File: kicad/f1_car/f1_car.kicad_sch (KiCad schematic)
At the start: 3 parts, among them U1 ESP32-DevKitC

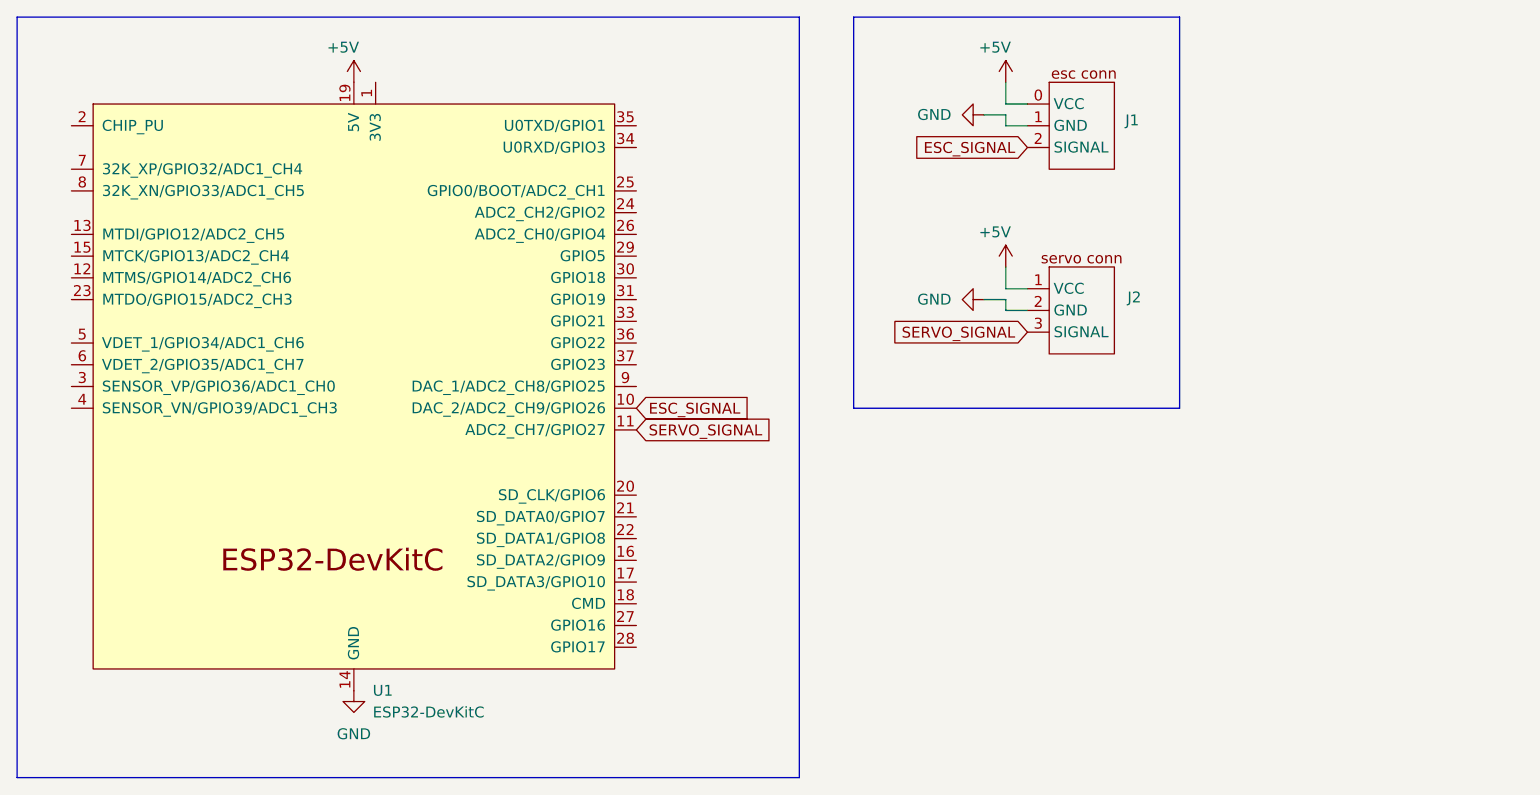
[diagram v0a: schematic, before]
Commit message: added limiter
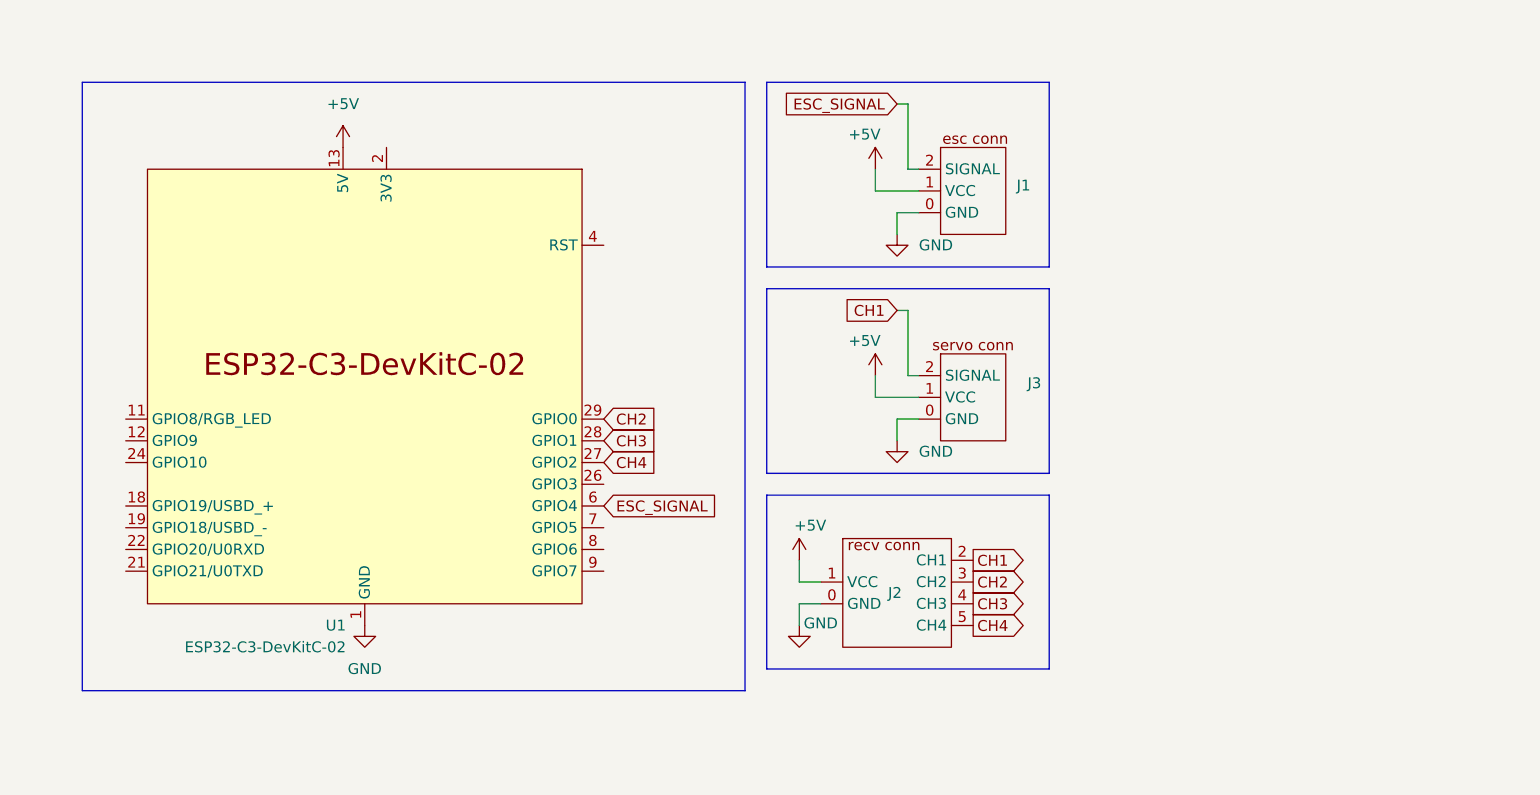
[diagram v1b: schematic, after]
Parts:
- removed J2: ~, symbol lib_progetto:steering_servo_connector
- removed U1: ESP32-DevKitC, PCM_Espressif:ESP32-DevKitC, symbol PCM_Espressif:ESP32-DevKitC
- added J2: ~, symbol lib_progetto:receiver_connector
- added J3: ~, symbol lib_progetto:steering_servo_connector
- added U1: ESP32-C3-DevKitC-02, PCM_Espressif:ESP32-C3-DevKitC-02, symbol PCM_Espressif:ESP32-C3-DevKitC-02
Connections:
- net +5V: now also J1.1 (VCC), J2.1 (VCC), J3.1 (VCC), U1.13 (5V), U1.14 (5V); no longer J1.0 (VCC)
- net ESC_SIGNAL: now also U1.6 (GPIO4)
- net GND: now also J1.0 (GND), J2.0 (GND), J3.0 (GND), U1.1 (GND), U1.10 (GND), U1.15 (GND), U1.16 (GND), U1.17 (GND), U1.20 (GND), U1.23 (GND), U1.25 (GND), U1.30 (GND), U1.5 (GND); no longer J1.1 (GND)
- new net 3V3: U1.2 (3V3), U1.3 (3V3)
- new net CH1: J2.2 (CH1), J3.2 (SIGNAL)
- new net CH2: J2.3 (CH2), U1.29 (GPIO0)
- new net CH3: J2.4 (CH3), U1.28 (GPIO1)
- new net CH4: J2.5 (CH4), U1.27 (GPIO2)
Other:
- moved on the sheet: J1

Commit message: schematic update
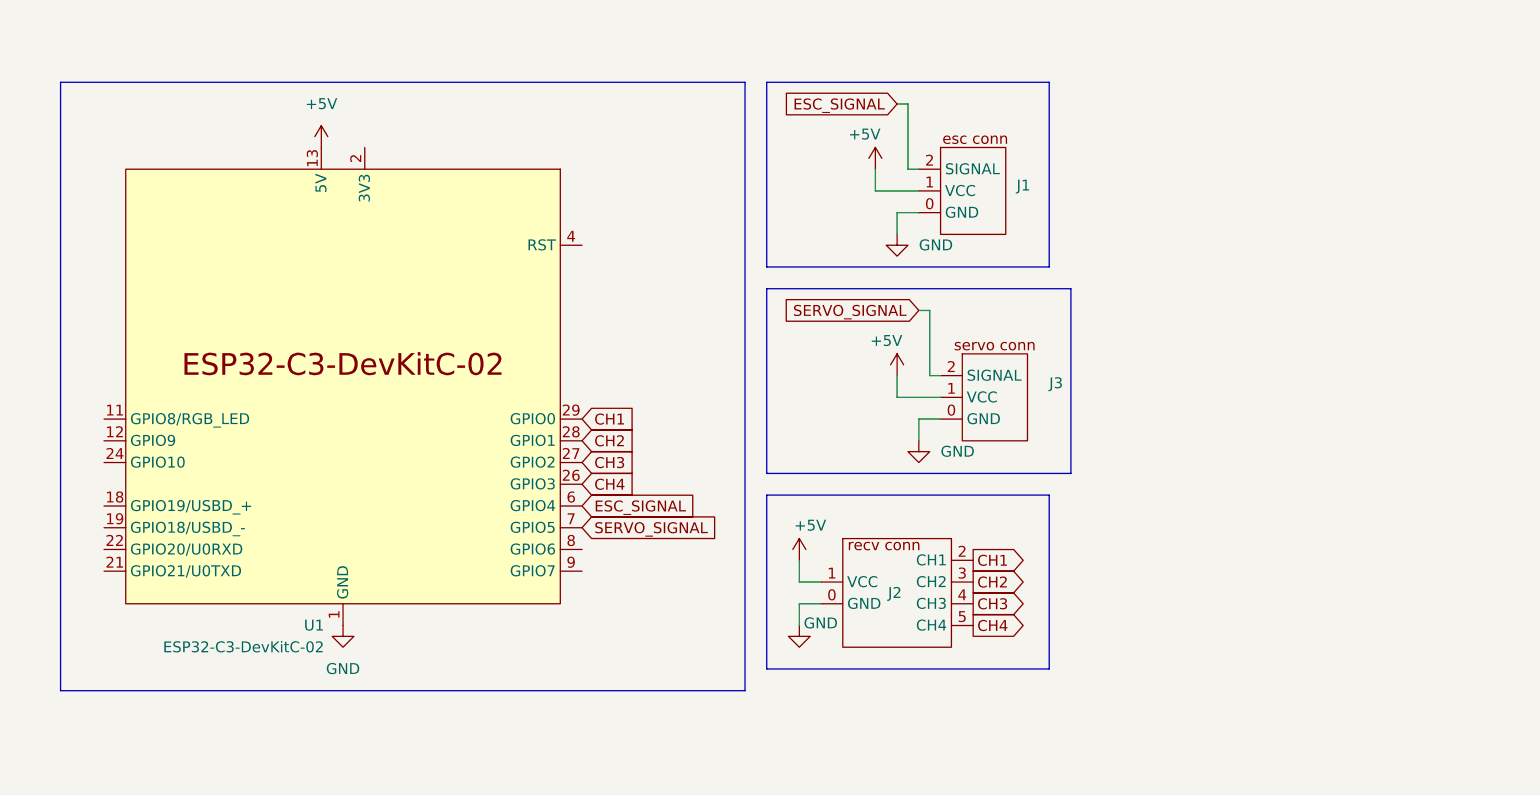
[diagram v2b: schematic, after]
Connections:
- net CH1: now also U1.29 (GPIO0); no longer J3.2 (SIGNAL)
- net CH2: now also U1.28 (GPIO1); no longer U1.29 (GPIO0)
- net CH3: now also U1.27 (GPIO2); no longer U1.28 (GPIO1)
- net CH4: now also U1.26 (GPIO3); no longer U1.27 (GPIO2)
- net SERVO_SIGNAL: now reaches U1.7 (GPIO5)
- net SERVO_SIGNAL: now also J3.2 (SIGNAL)
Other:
- moved on the sheet: J3, U1

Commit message: schematic pdf
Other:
- company: (none) -> ITIS E.MATTEI URBINO
- title: (none) -> F1 Car
- moved on the sheet: J1, J2, J3, U1

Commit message: pcb shield
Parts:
- removed J1: ~, symbol lib_progetto:esc_connector
- removed J2: ~, symbol lib_progetto:receiver_connector
- removed J3: ~, symbol lib_progetto:steering_servo_connector
- added J1: ~, symbol connettori_progetto:esc_conn
- added J2: ~, symbol connettori_progetto:recv_conn
- added J3: ~, symbol connettori_progetto:servo_conn
- added J4: Conn_01x12_Pin, Connector_PinHeader_2.54mm:PinHeader_2x06_P2.54mm_Horizontal, symbol Connector:Conn_01x12_Pin
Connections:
- net +5V: now also J1.2 (VCC), J2.2 (VCC), J3.2 (VCC), J4.11 (Pin_11), J4.3 (Pin_3), J4.4 (Pin_4)
- net CH1: now also J2.3 (CH1), J4.9 (Pin_9)
- net CH2: now also J2.4 (CH2), J4.7 (Pin_7)
- net CH3: now also J2.5 (CH3), J4.10 (Pin_10)
- net CH4: now also J2.6 (CH4), J4.8 (Pin_8)
- net ESC_SIGNAL: now also J1.3 (SIGNAL), J4.5 (Pin_5)
- net GND: now also J1.1 (GND), J2.1 (GND), J3.1 (GND), J4.1 (Pin_1), J4.12 (Pin_12), J4.2 (Pin_2)
- net SERVO_SIGNAL: now also J3.3 (SIGNAL), J4.6 (Pin_6)
- net 3V3 renamed +3V3
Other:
- company: ITIS E.MATTEI URBINO -> (none)
- title: F1 Car -> (none)
